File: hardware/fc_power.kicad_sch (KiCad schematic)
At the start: 35 parts, among them U3 LMR51430YFDDCR, U4 LMR51430YFDDCR, U6 LP5912-1.8DRVR, U7 LP5912-3.3DRVR

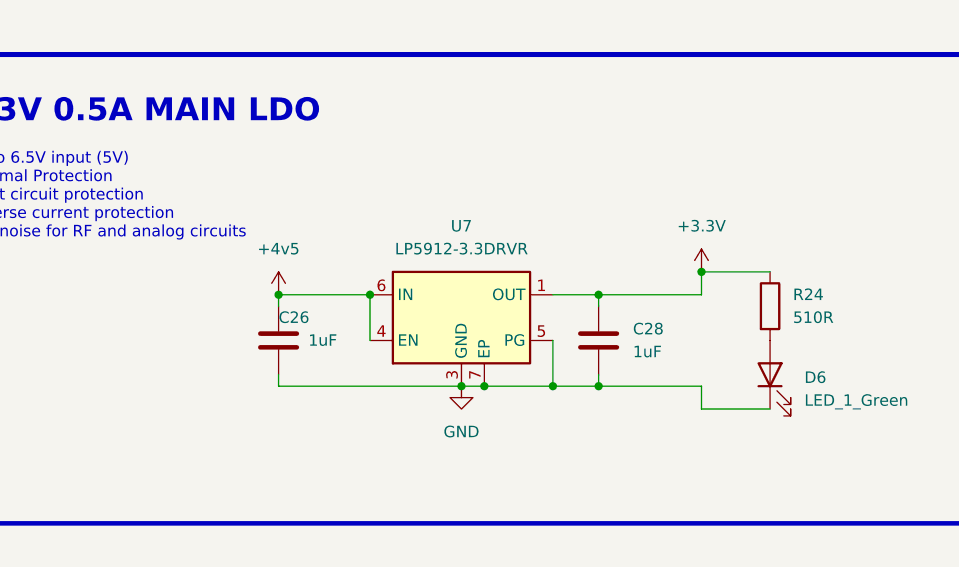
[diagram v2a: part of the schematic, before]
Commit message: Schematic: LGA nets per the R2a spec, S1/S2/B2/D7
- LGA (core_interface, generated by tools/lga_gen.py --sheet and re-saved by
  kicad-cli): J90/J91 get the 46 pins and nets of LGA_SPEC.md. 10V_ENABLE
  (B1), +3.3V (S1) and +10V (S2) no longer cross; PU0RX, SWDIO, SWCLK do.
- B2: SH-6 U12 pin 6 (DJI SBUS) leaves UART1_RX (ESP32-C3 TX) and joins
  PU0RX (RP2354A GPIO3, PIO UART0 RX); PU0RX becomes a global net so it
  crosses the LGA.
- D7: RP2354A SWCLK/SWDIO (U2.24/.25, no-connect before) go to the LGA and
  to TP32 SWCLK / TP31 SWDIO, 0.8 mm test pads on the Base (not in the BOM).
- S2: VTX pads move to the Base next to the SH-6: J41 +10V and J51 (was a
  second +10V pad on the Core) GND, on lib:SolderPad_1.2x1.2mm.
- S1: U7 LP5912-3.3 and its caps move to the Core (board assignment is by
  footprint, see the board commit). CIN C26 becomes the 0402 1 uF 25 V
  CL05A105KA5NQNC (C52923) the spec places; the 0201 was the R1 stop-gap.
- D6/R24, the green power LED, was on +3.3V on the Base, which no longer
  exists there. Instead of moving it to the Core or deleting it (spec
  section 2), R24 now takes +3V3 (TLV75533 U23, fed from the same +4v5):
  same LED, same parts, no Core space used.

ERC: 31 errors before and after, same types (bus_to_net_conflict 3,
hier_label_mismatch 1, pin_not_connected 1, pin_not_driven 16, pin_to_pin 1,
power_pin_not_driven 9). Netlist J90/J91 checked pad by pad against
lga_spec.json: 0 mismatches.

Co-Authored-By: Claude Opus 5.5 <noreply@anthropic.com>
Claude-Session: https://claude.ai/code/session_01KTp3FLjVXfXdWrkmr6af7d
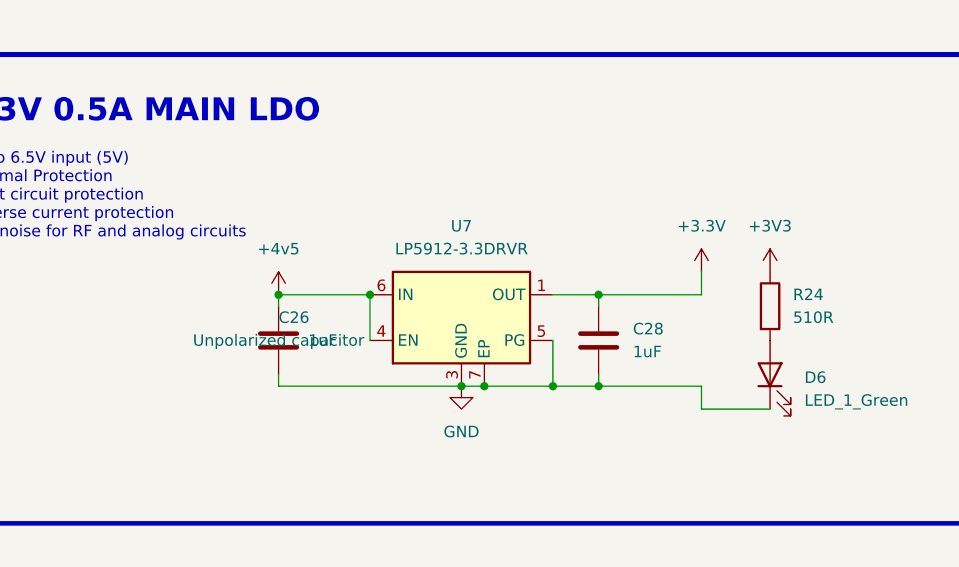
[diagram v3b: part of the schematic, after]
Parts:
- C26: footprint Capacitor_SMD:C_0201_0603Metric -> Capacitor_SMD:C_0402_1005Metric; LCSC C76935 -> C52923; MPN GRM033R61A105ME44D -> CL05A105KA5NQNC; Manufacturer Murata Electronics -> Samsung Electro-Mechanics
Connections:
- net +3.3V: no longer R24.1
- new net +3V3: R24.1
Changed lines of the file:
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@@
 	)
 	(junction
-		(at 245.11 116.84)
-		(diameter 0)
-		(color 0 0 0 0)
-	)
-	(junction
 		(at 259.08 57.15)
 		(diameter 0)
@@
 	(wire
 		(pts
-			(xy 245.11 116.84) (xy 252.73 116.84)
-		)
-		(stroke
-			(width 0)
-			(type default)
-		)
-	)
-	(wire
-		(pts
 			(xy 259.08 71.12) (xy 259.08 69.85)
 		)
@@
 			)
 		)
-		(property "Footprint" "Capacitor_SMD:C_0201_0603Metric"
+		(property "Footprint" "Capacitor_SMD:C_0402_1005Metric"
 			(at 199.0852 128.27 0)
 			(hide yes)
@@
 			)
 		)
-		(property "Description" ""
+		(property "Description" "Unpolarized capacitor"
 			(at 198.12 124.46 0)
 			(show_name no)
@@
 			)
 		)
-		(property "LCSC" "C76935"
+		(property "LCSC" "C52923"
 			(at 198.12 124.46 0)
 			(hide yes)
@@
 			)
 		)
-		(property "MPN" "GRM033R61A105ME44D"
+		(property "MPN" "CL05A105KA5NQNC"
 			(at 0 15.24 0)
 			(hide yes)
@@
 			)
 		)
-		(property "Manufacturer" "Murata Electronics"
+		(property "Manufacturer" "Samsung Electro-Mechanics"
 			(at 0 15.24 0)
 			(hide yes)
@@
 					(unit 1)
 				)
+			)
+		)
+	)
+	(symbol
+		(lib_id "power:+3V3")
+		(at 252.73 116.84 0)
+		(unit 1)
+		(body_style 1)
+		(exclude_from_sim no)
+		(in_bom yes)
+		(on_board yes)
+		(in_pos_files yes)
+		(dnp no)
+		(fields_autoplaced yes)
+		(property "Reference" "#PWR0290"
+			(at 252.73 120.65 0)
+			(hide yes)
+			(show_name no)
+			(do_not_autoplace no)
+			(effects
+				(font
+					(size 1.27 1.27)
+				)
+			)
+		)
+		(property "Value" "+3V3"
+			(at 252.73 111.76 0)
+			(show_name no)
+			(do_not_autoplace no)
+			(effects
+				(font
+					(size 1.27 1.27)
+				)
+			)
+		)
+		(property "Footprint" ""
+			(at 252.73 116.84 0)
+			(hide yes)
+			(show_name no)
+			(do_not_autoplace no)
+			(effects
+				(font
+					(size 1.27 1.27)
+				)
+			)
+		)
+		(property "Datasheet" ""
+			(at 252.73 116.84 0)
+			(hide yes)
+			(show_name no)
+			(do_not_autoplace no)
+			(effects
+				(font
+					(size 1.27 1.27)
+				)
+			)
+		)
+		(property "Description" "Power symbol creates a global label with name \"+3V3\""
+			(at 252.73 116.84 0)
+			(hide yes)
+			(show_name no)
+			(do_not_autoplace no)
+			(effects
+				(font
+					(size 1.27 1.27)
+				)
+			)
+		)
+		(pin "1"
+		)
+		(instances
+			(project "OpenAIO-Base"
+				(path "/fb88b6f9-ee39-4640-a9d4-04a17ceeac64/cdf44e0a-3675-4533-b9f5-78ffc381d2a5"
+					(reference "#PWR0290")
+					(unit 1)
+				)

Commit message: Base: power stage (shunt path, Kelvin sense, U4 HF cap)
- Shunt turned under the battery pad, ~23 vias in/around pad 2, /CSA+ feed
  kept free of vias and B tracks (named 'csa feed' rule areas, one notch for
  the U25 +3V3 via).
- INA186 (U25) + C104 on F next to the shunt; Kelvin taps at the inner pad
  edges, -IN B trace routed clear of the USB1 peg hole.
- C107 100 nF HF cap at U4 VIN (fc_power sheet).
- +3V3/CURR/+5V/USB GND re-routed out of the F +BATT corridor; D4/R21 moved
  under the Core; edge GND via moved into the USB shell pad.

Measured (DC solver, h 0.05 mm), HEAD 5b15929 -> this commit:
  /CSA+ path      0.897 -> 0.134 mOhm (no via > 2 A, was 21)
  Kelvin -IN      pick-up 0.035..0.171 -> 0 mOhm/A (copper error +42.3 % -> -7.7 % vs pad-mean model)
  +BATT mean      0.632 -> 0.630 mOhm
  GND mean        0.365 -> 0.361 mOhm
DRC (--refill-zones --schematic-parity): 0 unconnected, same error types as
HEAD; clearance 17 (17), copper_edge 4 (4), via_dangling 1 (1),
silk_over_copper 49 (34). ERC errors 31.

Co-Authored-By: Claude Opus 5.5 <noreply@anthropic.com>
Claude-Session: https://claude.ai/code/session_01KTp3FLjVXfXdWrkmr6af7d
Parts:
- added C107: 100nF, Capacitor_SMD:C_0402_1005Metric, symbol Device:C
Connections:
- net +BATT: now also C107.1
- net GND: now also C107.2

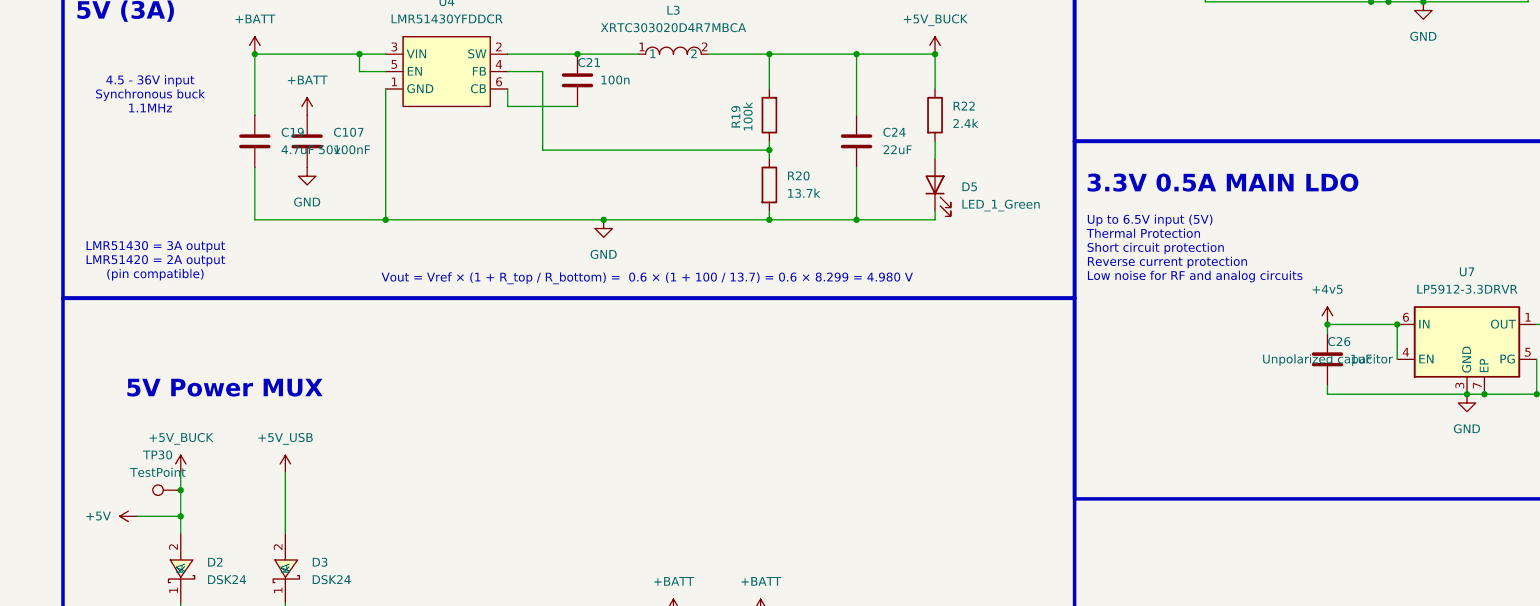
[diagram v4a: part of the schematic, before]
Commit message: Schematic readability: TP texts, C19/C107, C26, title blocks (FB5 item 6, V9-V11/M6)
- TestPoint values ('TestPoint') hidden on all sheets: the stacked TP16/TP17
  (root), TP24/TP25 and TP18/TP19/TP26/TP27 (RP2354A) texts no longer overlap.
- C19 reference/value moved left of the part (no longer printed over C107).
- C26 Description field hidden.
- Title blocks: rev r2, date 2026-10 (title added where missing) on the root,
  RP2354A, Power, IMU, OSD, Pads, ESC channel and Core interface sheets.
Edited with kicad-skip, re-saved with `kicad-cli sch upgrade --force` so the
diff stays minimal. Not done: rx_esp32c3_sx1281 and fc_blackbox title blocks
(they carry other projects' instances, OpenRX-Lite / BLACKBOX, and the headless
re-save renumbers their references); TP10 outside the frame (moving it would
detach its wire); N4 SPI0 label lift (label position is the connection point);
M7 net naming (+4v5 / +3.3V vs +3V3) left as is, it touches the LGA spec.
ERC 31 errors (unchanged).

Co-Authored-By: Claude Opus 5.5 <noreply@anthropic.com>
Claude-Session: https://claude.ai/code/session_01KTp3FLjVXfXdWrkmr6af7d
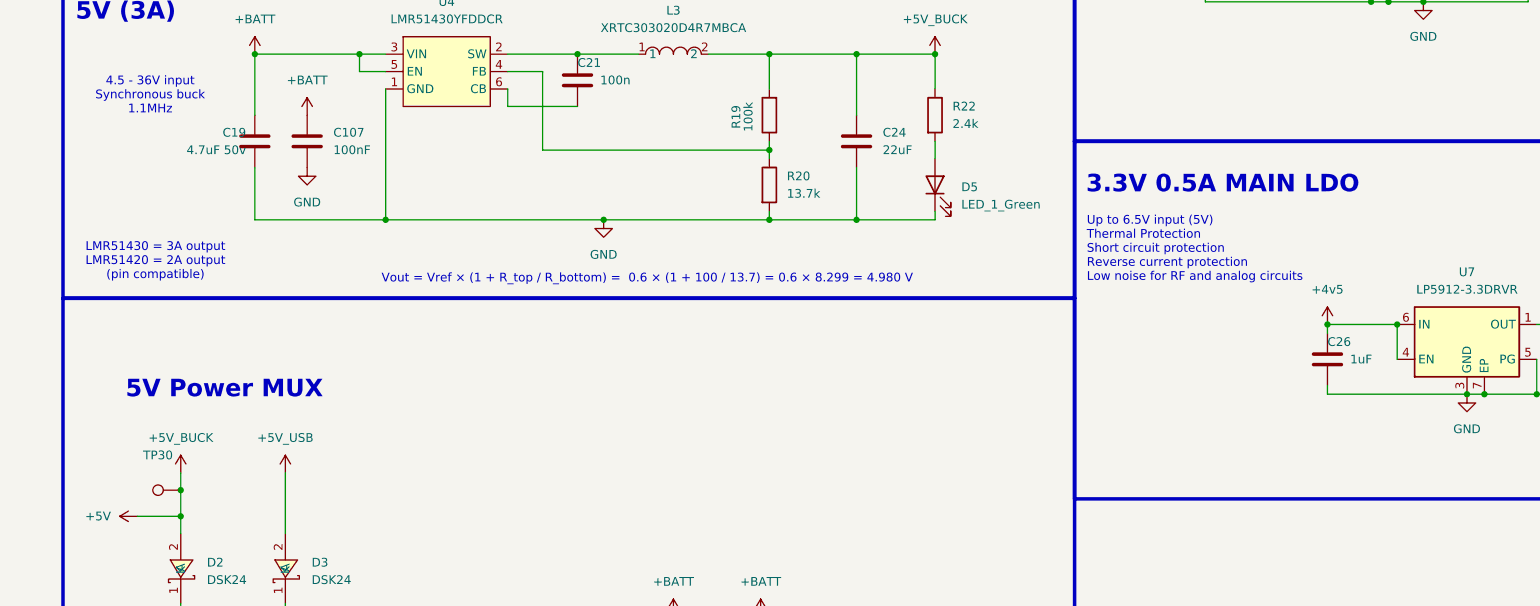
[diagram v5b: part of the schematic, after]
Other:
- title: (none) -> Power
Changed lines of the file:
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@@
 	(generator_version "10.0")
 	(paper "A4")
+	(title_block
+		(title "Power")
+		(date "2026-10")
+		(rev "r2")
+	)
 	(polyline
 		(pts
@@
 		(property "Description" "Unpolarized capacitor"
 			(at 198.12 124.46 0)
+			(hide yes)
 			(show_name no)
 			(do_not_autoplace no)
@@
 		(property "Value" "TestPoint"
 			(at 27.813 140.97 90)
+			(hide yes)
 			(show_name no)
 			(do_not_autoplace no)
@@
 		(fields_autoplaced yes)
 		(property "Reference" "C19"
-			(at 45.72 91.4399 0)
+			(at 40.64 91.4399 0)
 			(show_name no)
 			(do_not_autoplace no)
@@
 					(size 1.27 1.27)
 				)
-				(justify left)
+				(justify right)
 			)
 		)
 		(property "Value" "4.7uF 50v"
-			(at 45.72 93.9799 0)
+			(at 40.64 93.9799 0)
 			(show_name no)
 			(do_not_autoplace no)
@@
 					(size 1.27 1.27)
 				)
-				(justify left)
+				(justify right)
 			)
 		)

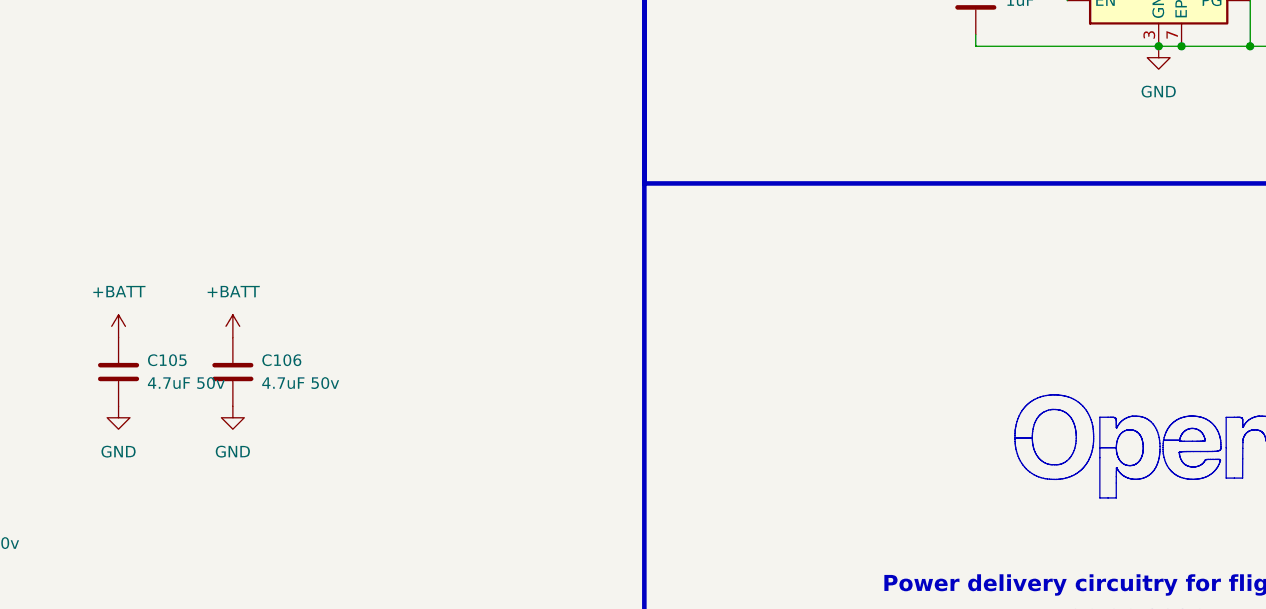
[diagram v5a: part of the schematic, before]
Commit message: ESC MCUs: battery-only +3V3_ESC from U27 TLV75533 on +5V (FB6 item 2, I3)
U27 TLV75533PDQNR (IN = EN = +5V, C110/C111 1uF 0201) makes +3V3_ESC for
U13/U15/U17/U19 VDD (pin 17) and their 16 ESC-side pins. Without a
battery the AT32s are now off, so they no longer drive the NSG2065Q
inputs while the gate-driver VCC (+10V) is 0 V. DRU: U27 mask-gang
exception (same as U23).

SD card +3V3 feed: via (69.12,69.30) -> In5 8.2 mm, inside the +10V pour
outline -> via (76.55,72.23). On In4 it cut the +BATT plane (0.596 mOhm).
+BATT measured 0.577 for In5, In2 and B.Cu and with the feed removed.
C36 restored on B (75.62,73.20).

Base identity texts are on B.Fab: there is no B.Cu GND pour spot for
0.5 mm knockout text >= 0.3 mm from pads (the only fit is under Rsense2).

Checks: Base DRC 20 (cl 15, edge 4, via_dangling 1, no new type),
parity 70; Core 27/7; ERC 31; unconnected 0/0; +BATT 0.577 mOhm (pw2
mean, 1700c87: 0.573); GND 0.356 mOhm; +5V 56.4 mV.

Co-Authored-By: Claude Opus 5.5 <noreply@anthropic.com>
Claude-Session: https://claude.ai/code/session_01KTp3FLjVXfXdWrkmr6af7d
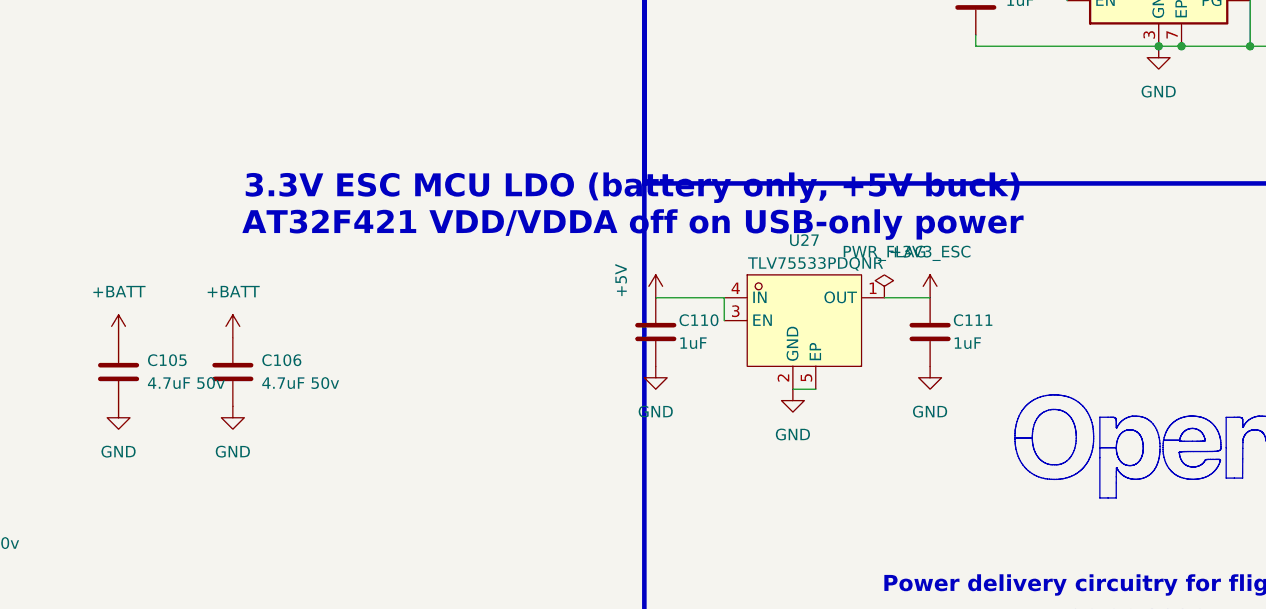
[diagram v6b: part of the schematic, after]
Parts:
- added C110, C111: 1uF, Capacitor_SMD:C_0201_0603Metric, symbol Device:C
- added U27: TLV75533PDQNR, OpenRX-Shared:X2SON-4_L1.0-W1.0-P0.65-TL-EP, symbol OpenRX-Shared:TLV75533PDQNR
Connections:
- net +5V: now also C110.1, U27.3 (EN), U27.4 (IN)
- net GND: now also C110.2, C111.2, U27.2 (GND), U27.5 (EP)
- new net +3V3_ESC: C111.1, U27.1 (OUT)
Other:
- note added: "3.3V ESC MCU LDO (battery only, +5V buck) AT32F421 VDD/VDDA off on USB-only power"

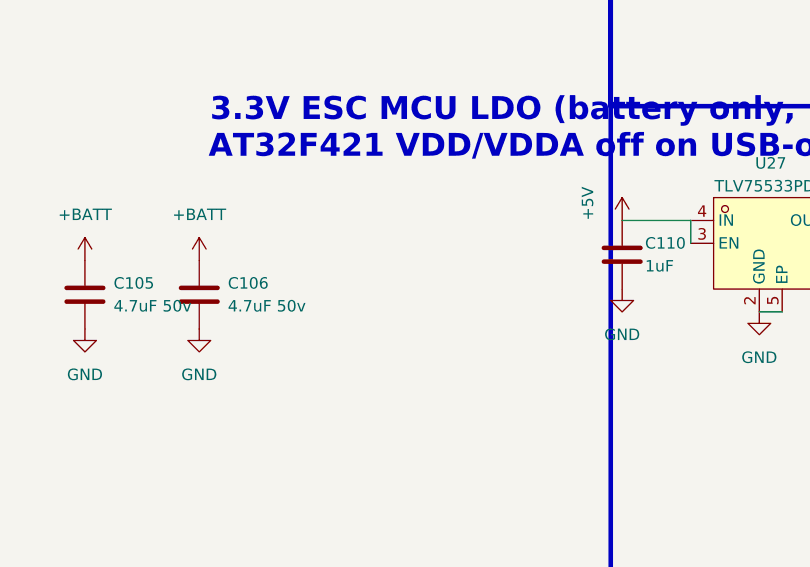
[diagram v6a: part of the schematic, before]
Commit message: +10V: two more 22 uF output caps beside C23 (FB8 T2)
C112/C113 (CL10A226MO7JZNC, Samsung, fields copied from C23) added to
fc_power and synced to the Base: B.Cu row next to C23, 0.205 mm body gaps,
+10V/GND 0.5 mm strips, GND pads 2.6/3.6 mm from U3.1. Effective
capacitance at 9.84 V 3.06 -> 9.2 uF (needs 10.9; no third site).

Room: C23 -0.11 mm; TP4 +1.0 mm with its via in the pad; J90.11 GND via
moved into the land (POFV) with In2 SPI0.MISO straightened and the B +5V
D2->R22 feed rerouted; SC2/SD2 labels to B.Fab (no silk spot).

Checks: Base DRC 20 (cl 15, edge 4, vd 1), parity nc 70 / missing 90,
Core 27/7, unconnected 0/0, ERC 31; +BATT 0.584, GND 0.357 mOhm,
+5V 56.4 mV.

Co-Authored-By: Claude Opus 5.5 <noreply@anthropic.com>
Claude-Session: https://claude.ai/code/session_01KTp3FLjVXfXdWrkmr6af7d
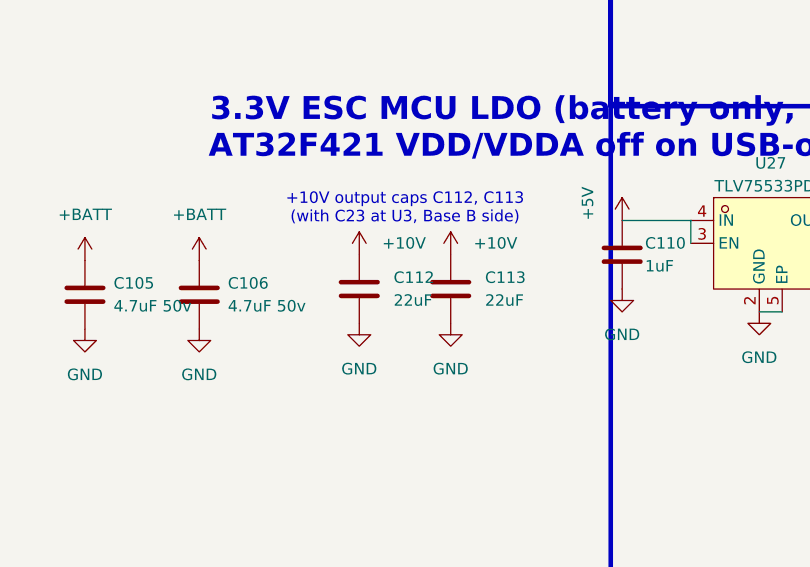
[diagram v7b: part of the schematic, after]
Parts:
- added C112, C113: 22uF, Capacitor_SMD:C_0603_1608Metric, symbol Device:C
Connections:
- net +10V: now also C112.1, C113.1
- net GND: now also C112.2, C113.2
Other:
- note added: "+10V output caps C112, C113 (with C23 at U3, Base B side)"
